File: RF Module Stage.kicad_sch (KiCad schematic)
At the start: 14 parts, among them IC1 SI5351A-B-GT, J10 TSM-106-01-L-SV, J7 BWSMA-KE-P001, J8 BWSMA-KE-P001, J9 BWSMA-KE-P001, Y2 ABM8G-25.000MHZ-B4Y-T3

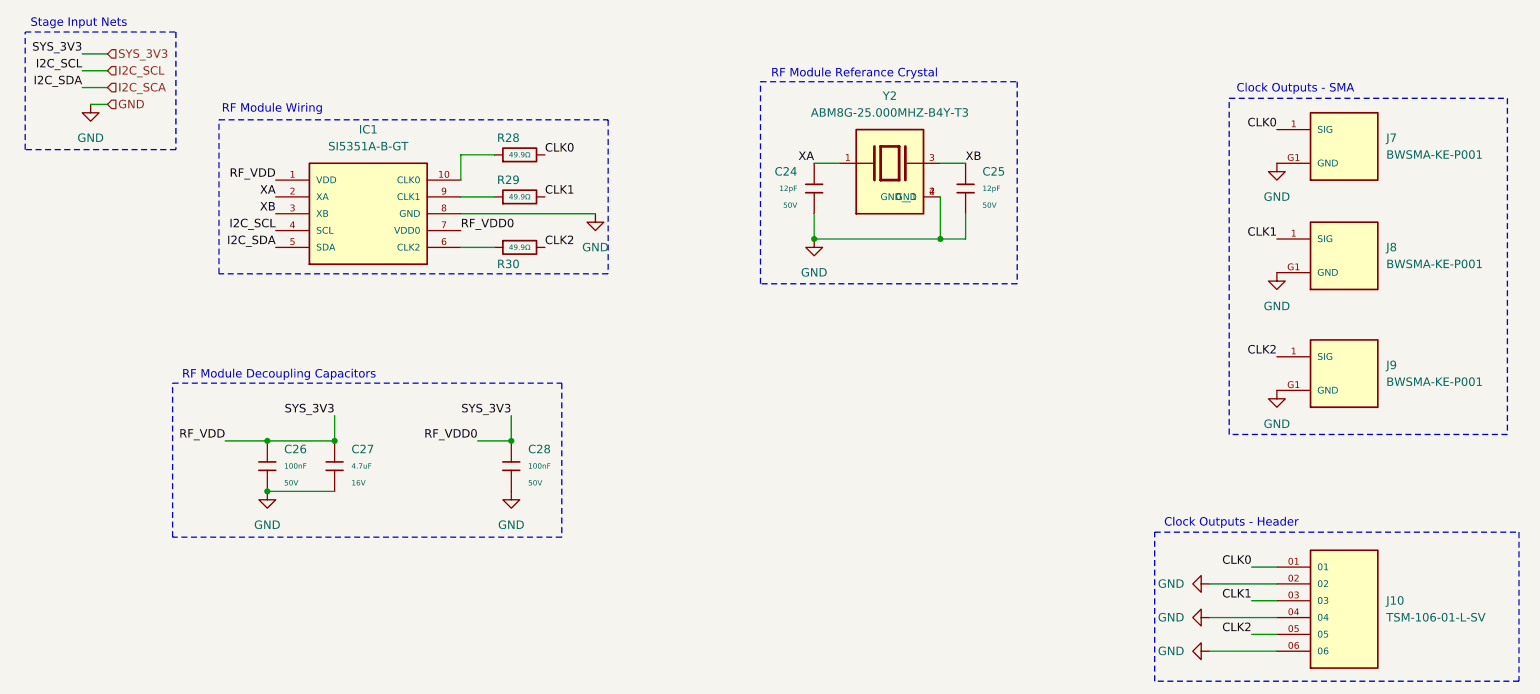
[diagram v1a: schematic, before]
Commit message: - Added Hysteresis resistor on TLV431BSN1T1G - Lowered TLV431BSN1T1G impedance values for resistors on the voltage divider
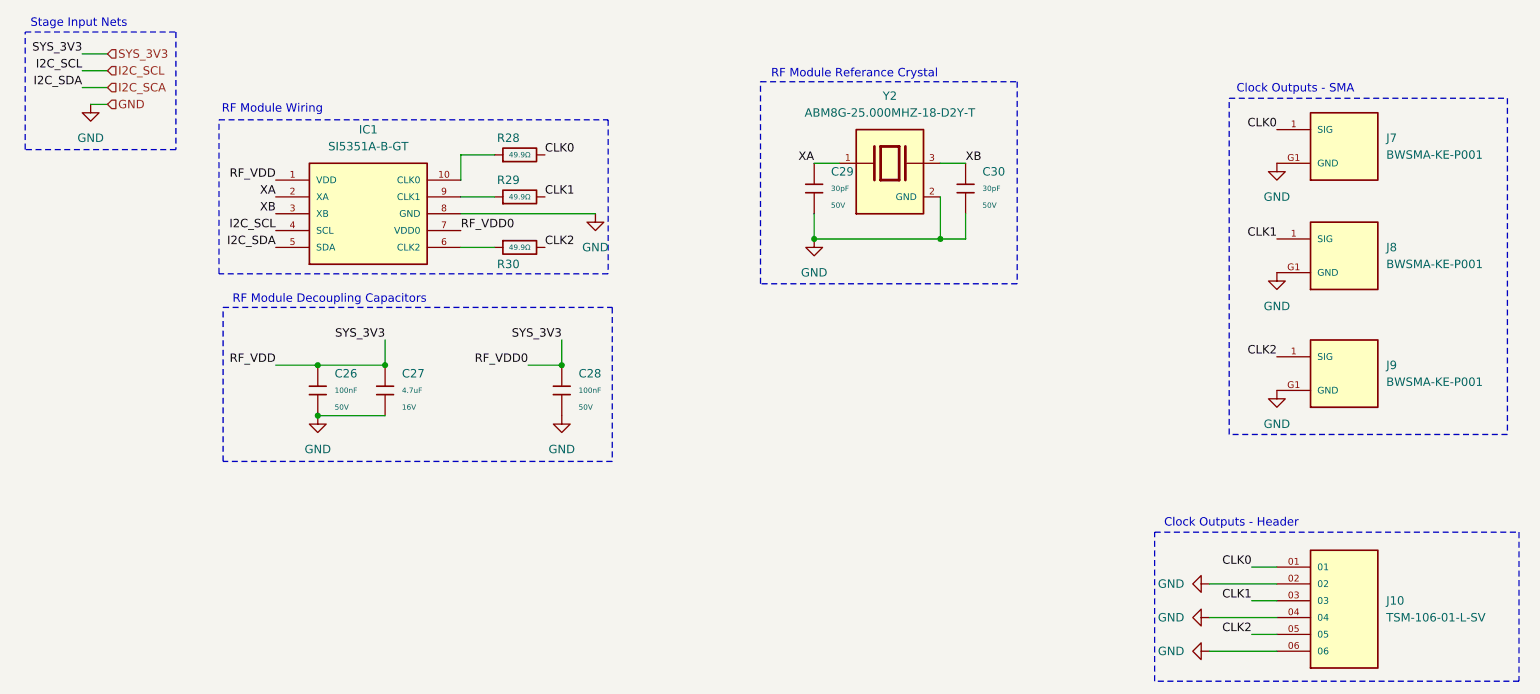
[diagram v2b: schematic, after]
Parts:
- removed C24, C25: 12pF, PCM_JLCPCB:C_0603, symbol PCM_JLCPCB-Capacitors:0603,12pF
- removed Y2: ABM8G-25.000MHZ-B4Y-T3, ABM8G-25.000MHZ-B4Y-T3:XTAL_ABM8G-25.000MHZ-B4Y-T3, symbol ABM8G-25.000MHZ-B4Y-T3:ABM8G-25.000MHZ-B4Y-T3
- added C29, C30: 30pF, PCM_JLCPCB:C_0603, symbol PCM_JLCPCB-Capacitors:0603,30pF
- added Y2: ABM8G-25.000MHZ-18-D2Y-T, Stock 25MHz:XTAL_ABM8G-25.000MHZ-18-D2Y-T, symbol ABM8G-25.000MHZ-18-D2Y-T:ABM8G-25.000MHZ-18-D2Y-T
- IC1: footprint SI5351A-B-GT:SOP50P490X110-10N -> Si5351A-B:SOP50P490X110-10N
- J10: footprint TSM-106-01-L-SV:SAMTEC_TSM-106-01-L-SV -> Samtec TSM_106_01_L_SV:SAMTEC_TSM-106-01-L-SV
- J7, J8, J9: footprint BWSMA-KE-P001:BATWIRELESS_BWSMA-KE-P001 -> SMA Headert - BWSMA-KE-P001:BATWIRELESS_BWSMA-KE-P001
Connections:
- net GND: now also C29.2, C30.2, Y2.2 (GND), Y2.4 (GND)
- net XA: now also C29.1, Y2.1
- net XB: now also C30.1, Y2.3
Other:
- company: Yaniv Lieberman -> (none)
- title: (none) -> Integrated Si5351A Module - RF Module Stage
- moved on the sheet: C26, C27, C28
